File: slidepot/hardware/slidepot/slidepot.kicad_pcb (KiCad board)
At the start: 2 copper layers, 17.8 x 92.7 mm, 3 parts, among them J1 Conn_01x05_Male, J2 Conn_01x02

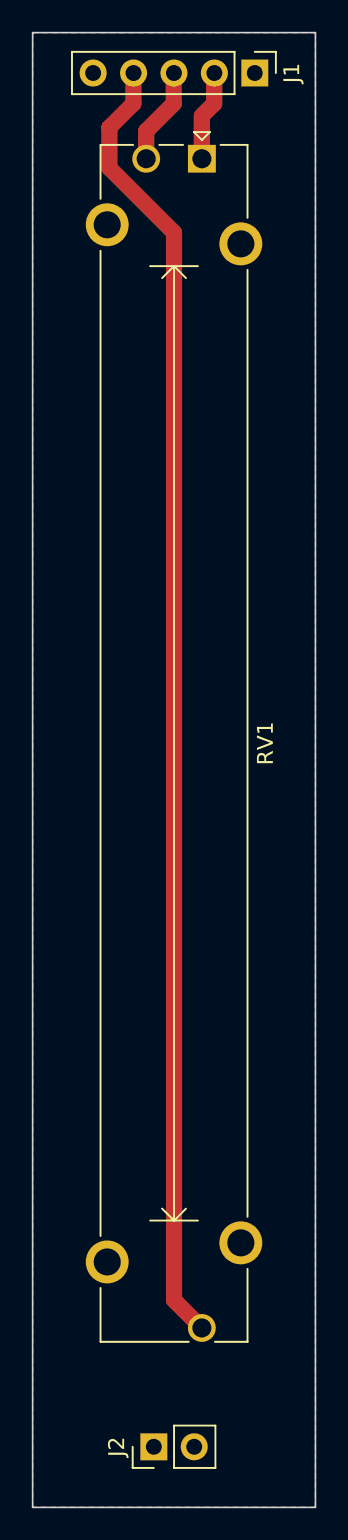
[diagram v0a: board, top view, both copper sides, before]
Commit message: Correct direction of input/output connectors for digital signals
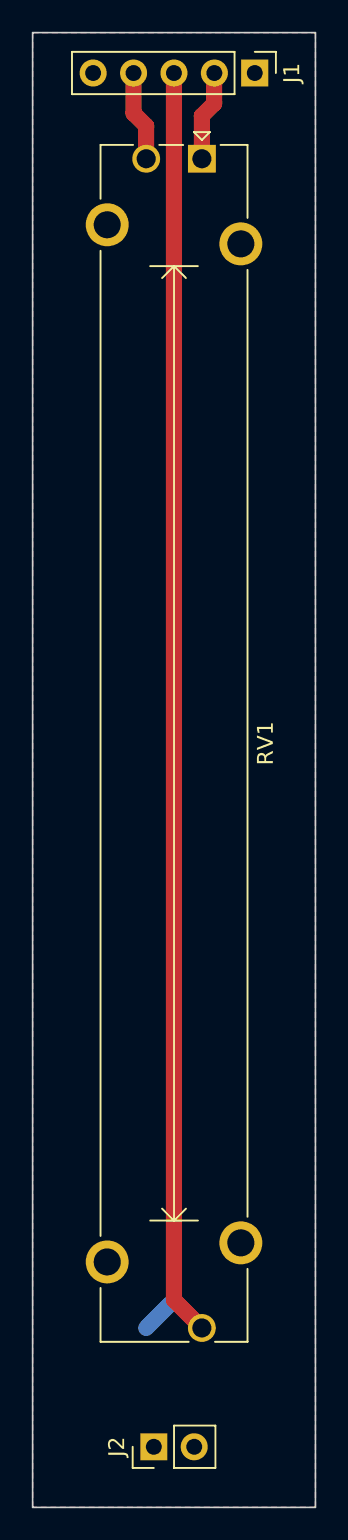
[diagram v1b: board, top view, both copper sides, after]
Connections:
- J1 pad 3: Net-(RV1-Pad2) -> Net-(RV1-Pad3)
- J1 pad 4: Net-(RV1-Pad3) -> Net-(RV1-Pad2)
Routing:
- net GND: track 0.00 -> 2.47 mm
- net Net-(RV1-Pad3): track 81.9 -> 79.6 mm
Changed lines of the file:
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@@
   )
   (net 0 "")
-  (net 1 "Net-(RV1-Pad1)")
+  (net 1 "Net-(J1-Pad2)")
   (net 2 "Net-(RV1-Pad2)")
   (net 3 "Net-(RV1-Pad3)")
@@
       (net 4 "GND") (pinfunction "Pin_1") (pintype "passive"))
     (pad "2" thru_hole oval (at 0 2.54 270) (size 1.7 1.7) (drill 1) (layers *.Cu *.Mask)
-      (net 1 "Net-(RV1-Pad1)") (pinfunction "Pin_2") (pintype "passive"))
+      (net 1 "Net-(J1-Pad2)") (pinfunction "Pin_2") (pintype "passive"))
     (pad "3" thru_hole oval (at 0 5.08 270) (size 1.7 1.7) (drill 1) (layers *.Cu *.Mask)
-      (net 2 "Net-(RV1-Pad2)") (pinfunction "Pin_3") (pintype "passive"))
+      (net 3 "Net-(RV1-Pad3)") (pinfunction "Pin_3") (pintype "passive"))
     (pad "4" thru_hole oval (at 0 7.62 270) (size 1.7 1.7) (drill 1) (layers *.Cu *.Mask)
-      (net 3 "Net-(RV1-Pad3)") (pinfunction "Pin_4") (pintype "passive"))
+      (net 2 "Net-(RV1-Pad2)") (pinfunction "Pin_4") (pintype "passive"))
     (pad "5" thru_hole oval (at 0 10.16 270) (size 1.7 1.7) (drill 1) (layers *.Cu *.Mask)
       (net 4 "GND") (pinfunction "Pin_5") (pintype "passive"))
@@
     (fp_circle (center 72.25 1.75) (end 73.25 1.75) (layer "F.Fab") (width 0.1) (fill none))
     (pad "1" thru_hole rect (at 0 0 270) (size 1.75 1.75) (drill 1.2) (layers *.Cu *.Mask)
-      (net 1 "Net-(RV1-Pad1)") (pinfunction "1") (pintype "passive"))
+      (net 1 "Net-(J1-Pad2)") (pinfunction "1") (pintype "passive"))
     (pad "2" thru_hole circle (at 0 3.5 270) (size 1.75 1.75) (drill 1.2) (layers *.Cu *.Mask)
       (net 2 "Net-(RV1-Pad2)") (pinfunction "2") (pintype "passive"))
@@
   (segment (start 167.625 45.72) (end 167.625 47.64) (width 1.016) (layer "F.Cu") (net 1))
   (segment (start 167.625 47.64) (end 166.85 48.415) (width 1.016) (layer "F.Cu") (net 1))
-  (segment (start 165.085 47.64) (end 163.35 49.375) (width 1.016) (layer "F.Cu") (net 2))
-  (segment (start 165.085 45.72) (end 165.085 47.64) (width 1.016) (layer "F.Cu") (net 2))
-  (segment (start 163.35 49.375) (end 163.35 51.11) (width 1.016) (layer "F.Cu") (net 2))
-  (segment (start 162.545 45.72) (end 162.545 47.64) (width 1.016) (layer "F.Cu") (net 3))
-  (segment (start 162.545 47.64) (end 161.036 49.149) (width 1.016) (layer "F.Cu") (net 3))
-  (segment (start 161.036 51.689) (end 165.1 55.753) (width 1.016) (layer "F.Cu") (net 3))
-  (segment (start 161.036 49.149) (end 161.036 51.689) (width 1.016) (layer "F.Cu") (net 3))
-  (segment (start 165.1 122.86) (end 166.85 124.61) (width 1.016) (layer "F.Cu") (net 3))
-  (segment (start 165.1 55.753) (end 165.1 122.86) (width 1.016) (layer "F.Cu") (net 3))
+  (segment (start 162.555 48.255) (end 162.555 45.72) (width 1.016) (layer "F.Cu") (net 2))
+  (segment (start 163.35 51.11) (end 163.35 49.05) (width 1.016) (layer "F.Cu") (net 2))
+  (segment (start 163.35 49.05) (end 162.555 48.255) (width 1.016) (layer "F.Cu") (net 2))
+  (segment (start 165.095 122.855) (end 166.85 124.61) (width 1.016) (layer "F.Cu") (net 3))
+  (segment (start 165.095 45.72) (end 165.095 122.855) (width 1.016) (layer "F.Cu") (net 3))
+  (segment (start 165.1 122.86) (end 163.35 124.61) (width 1.016) (layer "B.Cu") (net 4))
   (zone (net 4) (net_name "GND") (layers F&B.Cu) (hatch edge 0.508)
     (connect_pads (clearance 0.508))
